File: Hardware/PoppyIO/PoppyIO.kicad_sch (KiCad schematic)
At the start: 244 parts, among them J1 WAGO 233-504, J10 Phoenix MPT 0,5/ 4-2,54, J11 TC2030-IDC, J12 Conn_02x06_Odd_Even, J2 WAGO 233-504, J3 WAGO 233-504, J4 WAGO 233-504, J5 WAGO 233-504, J6 WAGO 233-504, J7 WAGO 233-504, J8 WAGO 233-504, SW1 PTS645SH43SMTR92LFS, U1 Pico, U10 74HC14, U11 74HC14, U12 74HC14, U2 PCA9538PW, U3 PCA9538PW, U4 PCA9538PW, U5 PCA9538PW, U6 ULN2003AD, U7 ULN2003AD, U8 ULN2003AD, U9 74HC14

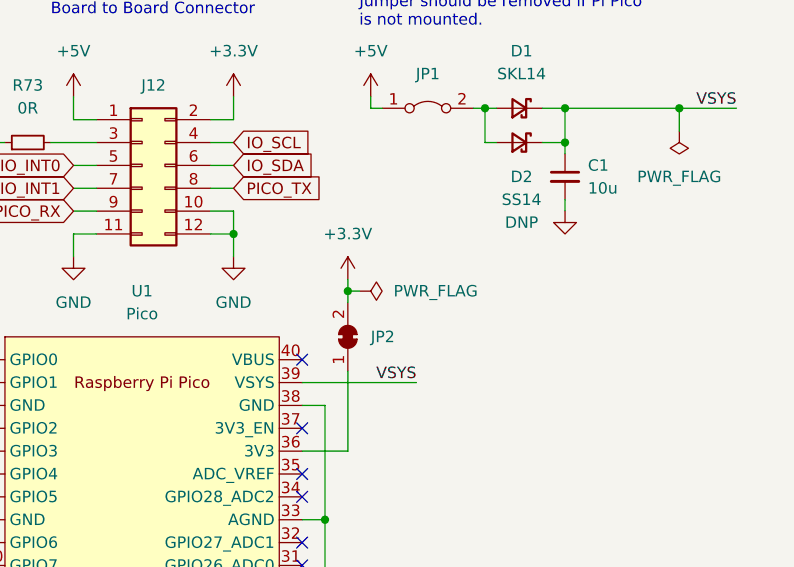
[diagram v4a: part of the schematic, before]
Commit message: hw: io: Update JP2
shouldn't be a solder jumper
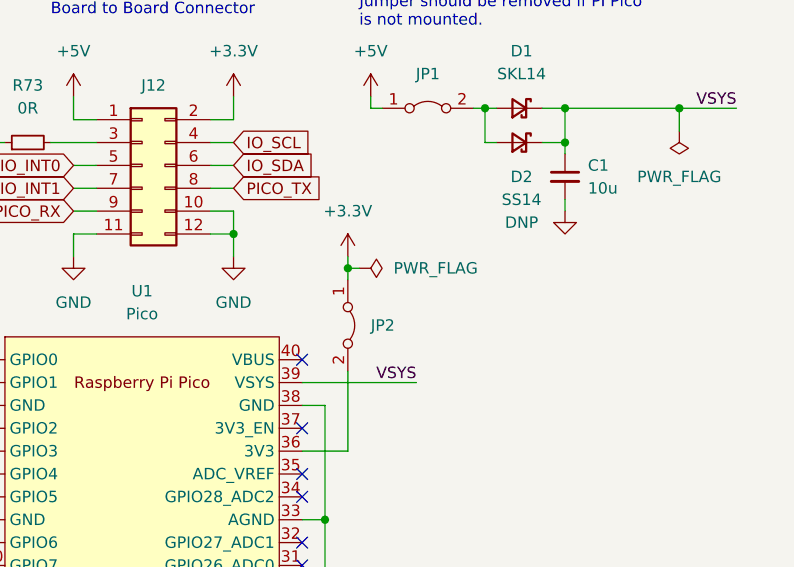
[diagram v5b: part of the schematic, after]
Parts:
- removed JP2: SolderJumper_2_Bridged, Jumper:SolderJumper-2_P1.3mm_Bridged_RoundedPad1.0x1.5mm, symbol Jumper:SolderJumper_2_Bridged
- added JP2: (no value), symbol Jumper:Jumper_2_Bridged
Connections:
- net +3V3: now also JP2.1 (A)
- net at U1.36 (3V3): now also JP2.2 (B)
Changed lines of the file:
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@@
   (junction (at 383.54 247.65) (diameter 0) (color 0 0 0 0)
   )
-  (junction (at 359.41 49.53) (diameter 0) (color 0 0 0 0)
+  (junction (at 359.41 46.99) (diameter 0) (color 0 0 0 0)
   )
   (junction (at 386.08 236.22) (diameter 0) (color 0 0 0 0)
@@
     (stroke (width 0) (type default) (color 0 0 0 0))
   )
-  (wire (pts (xy 359.41 49.53) (xy 360.68 49.53))
+  (wire (pts (xy 359.41 46.99) (xy 360.68 46.99))
     (stroke (width 0) (type default) (color 0 0 0 0))
   )
@@
     (stroke (width 0) (type default) (color 0 0 0 0))
   )
-  (wire (pts (xy 359.41 48.26) (xy 359.41 49.53))
+  (wire (pts (xy 359.41 45.72) (xy 359.41 46.99))
     (stroke (width 0) (type default) (color 0 0 0 0))
   )
@@
     (stroke (width 0) (type default) (color 0 0 0 0))
   )
-  (wire (pts (xy 359.41 49.53) (xy 359.41 50.8))
+  (wire (pts (xy 359.41 46.99) (xy 359.41 48.26))
     (stroke (width 0) (type default) (color 0 0 0 0))
   )
@@
     (pin "1")
   )
-  (symbol (lib_id "power:PWR_FLAG") (at 360.68 49.53 270) (unit 1)
+  (symbol (lib_id "power:PWR_FLAG") (at 360.68 46.99 270) (unit 1)
     (in_bom yes) (on_board yes) (fields_autoplaced)
-    (property "Reference" "#FLG0104" (id 0) (at 362.585 49.53 0)
+    (property "Reference" "#FLG0104" (id 0) (at 362.585 46.99 0)
       (effects (font (size 1.27 1.27)) hide)
     )
-    (property "Value" "PWR_FLAG" (id 1) (at 364.49 49.5299 90)
+    (property "Value" "PWR_FLAG" (id 1) (at 364.49 46.9899 90)
       (effects (font (size 1.27 1.27)) (justify left))
     )
-    (property "Footprint" "" (id 2) (at 360.68 49.53 0)
+    (property "Footprint" "" (id 2) (at 360.68 46.99 0)
       (effects (font (size 1.27 1.27)) hide)
     )
-    (property "Datasheet" "~" (id 3) (at 360.68 49.53 0)
+    (property "Datasheet" "~" (id 3) (at 360.68 46.99 0)
       (effects (font (size 1.27 1.27)) hide)
     )
@@
     (pin "1")
   )
-  (symbol (lib_id "power:+3.3V") (at 359.41 48.26 0) (unit 1)
+  (symbol (lib_id "power:+3.3V") (at 359.41 45.72 0) (unit 1)
     (in_bom yes) (on_board yes) (fields_autoplaced)
-    (property "Reference" "#PWR06" (id 0) (at 359.41 52.07 0)
+    (property "Reference" "#PWR06" (id 0) (at 359.41 49.53 0)
       (effects (font (size 1.27 1.27)) hide)
     )
-    (property "Value" "+3.3V" (id 1) (at 359.41 43.18 0))
-    (property "Footprint" "" (id 2) (at 359.41 48.26 0)
+    (property "Value" "+3.3V" (id 1) (at 359.41 40.64 0))
+    (property "Footprint" "" (id 2) (at 359.41 45.72 0)
       (effects (font (size 1.27 1.27)) hide)
     )
-    (property "Datasheet" "" (id 3) (at 359.41 48.26 0)
+    (property "Datasheet" "" (id 3) (at 359.41 45.72 0)
       (effects (font (size 1.27 1.27)) hide)
     )
@@
     (pin "7")
   )
-  (symbol (lib_id "Jumper:SolderJumper_2_Bridged") (at 359.41 54.61 270) (mirror x) (unit 1)
-    (in_bom yes) (on_board yes) (fields_autoplaced)
-    (property "Reference" "JP2" (id 0) (at 361.95 54.6099 90)
-      (effects (font (size 1.27 1.27)) (justify left))
-    )
-    (property "Value" "SolderJumper_2_Bridged" (id 1) (at 363.22 54.61 0)
-      (effects (font (size 1.27 1.27)) hide)
-    )
-    (property "Footprint" "Jumper:SolderJumper-2_P1.3mm_Bridged_RoundedPad1.0x1.5mm" (id 2) (at 359.41 54.61 0)
-      (effects (font (size 1.27 1.27)) hide)
-    )
-    (property "Datasheet" "~" (id 3) (at 359.41 54.61 0)
-      (effects (font (size 1.27 1.27)) hide)
-    )
-    (pin "1")
-    (pin "2")
-  )
   (symbol (lib_id "power:GND") (at 127 111.76 0) (unit 1)
     (in_bom yes) (on_board yes) (fields_autoplaced)
@@
     (pin "1")
   )
+  (symbol (lib_id "Jumper:Jumper_2_Bridged") (at 359.41 53.34 270) (unit 1)
+    (in_bom yes) (on_board yes) (fields_autoplaced)
+    (property "Reference" "JP2" (id 0) (at 361.95 53.3399 90)
+      (effects (font (size 1.27 1.27)) (justify left))
+    )
+    (property "Value" "" (id 1) (at 363.22 53.34 0)
+      (effects (font (size 1.27 1.27)) hide)
+    )
+    (property "Footprint" "" (id 2) (at 359.41 53.34 0)
+      (effects (font (size 1.27 1.27)) hide)
+    )
+    (property "Datasheet" "~" (id 3) (at 359.41 53.34 0)
+      (effects (font (size 1.27 1.27)) hide)
+    )
+    (pin "1")
+    (pin "2")
+  )
   (symbol (lib_id "Connector:TestPoint_Small") (at 66.04 228.6 0) (unit 1)
     (in_bom yes) (on_board yes)
@@
   (symbol (lib_id "power:+5V") (at 361.95 27.94 0) (unit 1)
     (in_bom yes) (on_board yes) (fields_autoplaced)
-    (property "Reference" "#PWR?" (id 0) (at 361.95 31.75 0)
+    (property "Reference" "#PWR0131" (id 0) (at 361.95 31.75 0)
       (effects (font (size 1.27 1.27)) hide)
     )
@@
       (reference "#PWR0130") (unit 1) (value "GND") (footprint "")
     )
+    (path "/f9200ee4-0053-410d-bc5c-53542c90d30e"
+      (reference "#PWR0131") (unit 1) (value "+5V") (footprint "")
+    )
     (path "/fb0963c8-0aa6-46ce-85a9-5d5af03b6001"
       (reference "#PWR0132") (unit 1) (value "+3.3V") (footprint "")
@@
       (reference "#PWR0143") (unit 1) (value "GND") (footprint "")
     )
-    (path "/f9200ee4-0053-410d-bc5c-53542c90d30e"
-      (reference "#PWR?") (unit 1) (value "+5V") (footprint "")
-    )
     (path "/b9ac49ae-7d34-4ed6-a926-b142ee48d81a"
       (reference "C1") (unit 1) (value "10u") (footprint "Capacitor_SMD:C_1210_3225Metric")
@@
       (reference "JP1") (unit 1) (value "~") (footprint "Connector_PinHeader_2.54mm:PinHeader_1x02_P2.54mm_Vertical")
     )
-    (path "/65d06c52-607b-438a-b9af-c2ce24e1e331"
-      (reference "JP2") (unit 1) (value "SolderJumper_2_Bridged") (footprint "Jumper:SolderJumper-2_P1.3mm_Bridged_RoundedPad1.0x1.5mm")
+    (path "/6612fd9a-51b0-4f77-bfea-9b018a73204f"
+      (reference "JP2") (unit 1) (value "~") (footprint "Connector_PinHeader_2.54mm:PinHeader_1x02_P2.54mm_Vertical")
     )
     (path "/d683efa9-3a6b-4bcc-9f90-fb444ca2faef"

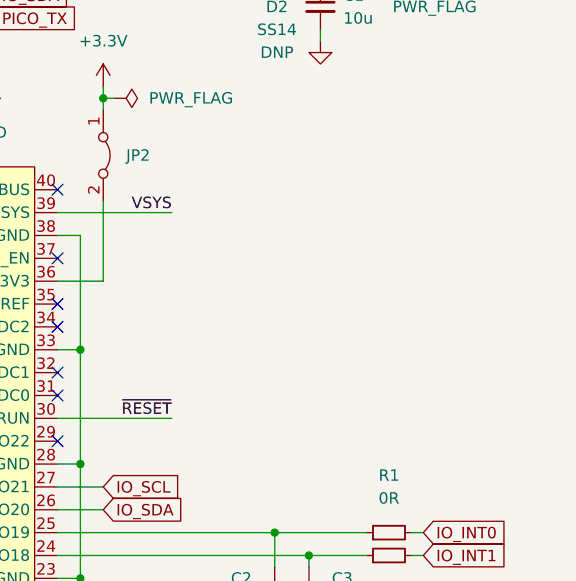
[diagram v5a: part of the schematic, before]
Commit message: hw: io: Add footprints for 3V3 decoupling caps
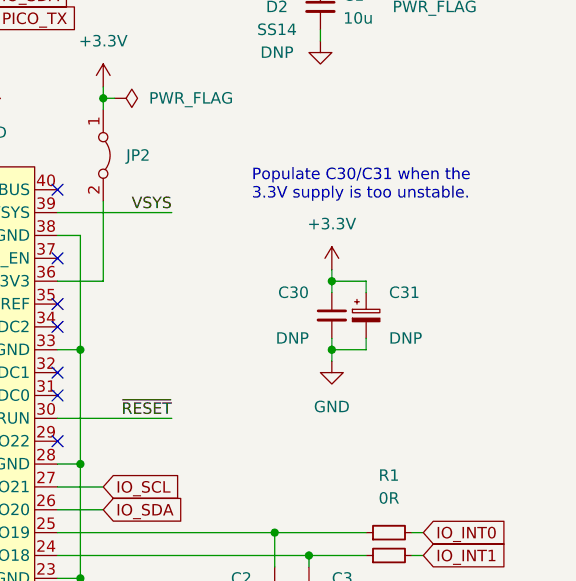
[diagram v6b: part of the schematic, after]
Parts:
- added C30: (no value), symbol Device:C_Small
- added C31: (no value), symbol Device:C_Polarized_Small
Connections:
- net +3V3: now also C30.1, C31.1
- net GND: now also C30.2, C31.2
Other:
- note added: "Populate C30/C31 when the 3.3V supply is too unstable."
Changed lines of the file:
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@@
   (junction (at 256.54 182.88) (diameter 0) (color 0 0 0 0)
   )
+  (junction (at 384.81 67.31) (diameter 0) (color 0 0 0 0)
+  )
   (junction (at 255.27 231.14) (diameter 0) (color 0 0 0 0)
   )
@@
   (junction (at 295.91 144.78) (diameter 0) (color 0 0 0 0)
   )
+  (junction (at 384.81 74.93) (diameter 0) (color 0 0 0 0)
+  )
   (junction (at 396.24 151.13) (diameter 0) (color 0 0 0 0)
   )
@@
     (stroke (width 0) (type default) (color 0 0 0 0))
   )
+  (wire (pts (xy 384.81 74.93) (xy 388.62 74.93))
+    (stroke (width 0) (type default) (color 0 0 0 0))
+  )
   (wire (pts (xy 186.69 255.27) (xy 187.96 255.27))
     (stroke (width 0) (type default) (color 0 0 0 0))
@@
     (stroke (width 0) (type default) (color 0 0 0 0))
   )
+  (wire (pts (xy 384.81 67.31) (xy 388.62 67.31))
+    (stroke (width 0) (type default) (color 0 0 0 0))
+  )
   (wire (pts (xy 243.84 255.27) (xy 245.11 255.27))
     (stroke (width 0) (type default) (color 0 0 0 0))
@@
     (stroke (width 0) (type default) (color 0 0 0 0))
   )
+  (wire (pts (xy 384.81 66.04) (xy 384.81 67.31))
+    (stroke (width 0) (type default) (color 0 0 0 0))
+  )
   (wire (pts (xy 255.27 241.3) (xy 251.46 241.3))
     (stroke (width 0) (type default) (color 0 0 0 0))
@@
     (stroke (width 0) (type default) (color 0 0 0 0))
   )
+  (wire (pts (xy 388.62 67.31) (xy 388.62 68.58))
+    (stroke (width 0) (type default) (color 0 0 0 0))
+  )
   (wire (pts (xy 210.82 229.87) (xy 210.82 231.14))
     (stroke (width 0) (type default) (color 0 0 0 0))
@@
     (stroke (width 0) (type default) (color 0 0 0 0))
   )
+  (wire (pts (xy 388.62 73.66) (xy 388.62 74.93))
+    (stroke (width 0) (type default) (color 0 0 0 0))
+  )
   (wire (pts (xy 82.55 95.25) (xy 82.55 105.41))
     (stroke (width 0) (type default) (color 0 0 0 0))
@@
     (stroke (width 0) (type default) (color 0 0 0 0))
   )
+  (wire (pts (xy 384.81 68.58) (xy 384.81 67.31))
+    (stroke (width 0) (type default) (color 0 0 0 0))
+  )
   (wire (pts (xy 194.31 41.91) (xy 195.58 41.91))
     (stroke (width 0) (type default) (color 0 0 0 0))
@@
     (stroke (width 0) (type default) (color 0 0 0 0))
   )
+  (wire (pts (xy 384.81 74.93) (xy 384.81 76.2))
+    (stroke (width 0) (type default) (color 0 0 0 0))
+  )
   (polyline (pts (xy 290.83 67.31) (xy 290.83 88.9))
     (stroke (width 0) (type default) (color 0 0 0 0))
@@
     (stroke (width 0) (type default) (color 0 0 0 0))
   )
+  (wire (pts (xy 384.81 73.66) (xy 384.81 74.93))
+    (stroke (width 0) (type default) (color 0 0 0 0))
+  )
   (wire (pts (xy 149.86 95.25) (xy 153.67 95.25))
     (stroke (width 0) (type default) (color 0 0 0 0))
@@
     (effects (font (size 1.27 1.27)) (justify right bottom))
   )
+  (text "Populate C30/C31 when the\n3.3V supply is too unstable."
+    (at 375.92 58.42 0)
+    (effects (font (size 1.27 1.27)) (justify left bottom))
+  )
   (text "V_{f}≅2.4V\nI=1mA" (at 91.44 172.72 0)
     (effects (font (size 1.27 1.27)) (justify left bottom))
@@
     (pin "1")
   )
+  (symbol (lib_id "power:+3.3V") (at 384.81 66.04 0) (unit 1)
+    (in_bom yes) (on_board yes) (fields_autoplaced)
+    (property "Reference" "#PWR094" (id 0) (at 384.81 69.85 0)
+      (effects (font (size 1.27 1.27)) hide)
+    )
+    (property "Value" "+3.3V" (id 1) (at 384.81 60.96 0))
+    (property "Footprint" "" (id 2) (at 384.81 66.04 0)
+      (effects (font (size 1.27 1.27)) hide)
+    )
+    (property "Datasheet" "" (id 3) (at 384.81 66.04 0)
+      (effects (font (size 1.27 1.27)) hide)
+    )
+    (pin "1")
+  )
   (symbol (lib_id "power:GND") (at 334.01 240.03 0) (unit 1)
     (in_bom yes) (on_board yes) (fields_autoplaced)
@@
     (pin "9")
   )
+  (symbol (lib_id "Device:C_Small") (at 384.81 71.12 0) (unit 1)
+    (in_bom yes) (on_board yes) (fields_autoplaced)
+    (property "Reference" "C30" (id 0) (at 382.27 68.5862 0)
+      (effects (font (size 1.27 1.27)) (justify right))
+    )
+    (property "Value" "" (id 1) (at 382.27 71.1262 0)
+      (effects (font (size 1.27 1.27)) (justify right))
+    )
+    (property "Footprint" "" (id 2) (at 384.81 71.12 0)
+      (effects (font (size 1.27 1.27)) hide)
+    )
+    (property "Datasheet" "~" (id 3) (at 384.81 71.12 0)
+      (effects (font (size 1.27 1.27)) hide)
+    )
+    (property "Config" "DNP" (id 4) (at 382.27 73.6662 0)
+      (effects (font (size 1.27 1.27)) (justify right))
+    )
+    (pin "1")
+    (pin "2")
+  )
   (symbol (lib_id "Device:LED_Small") (at 83.82 196.85 90) (unit 1)
     (in_bom yes) (on_board yes) (fields_autoplaced)
@@
     (pin "2")
   )
+  (symbol (lib_id "power:GND") (at 384.81 76.2 0) (unit 1)
+    (in_bom yes) (on_board yes) (fields_autoplaced)
+    (property "Reference" "#PWR096" (id 0) (at 384.81 82.55 0)
+      (effects (font (size 1.27 1.27)) hide)
+    )
+    (property "Value" "GND" (id 1) (at 384.81 81.28 0))
+    (property "Footprint" "" (id 2) (at 384.81 76.2 0)
+      (effects (font (size 1.27 1.27)) hide)
+    )
+    (property "Datasheet" "" (id 3) (at 384.81 76.2 0)
+      (effects (font (size 1.27 1.27)) hide)
+    )
+    (pin "1")
+  )
   (symbol (lib_id "power:GND") (at 128.27 242.57 0) (unit 1)
     (in_bom yes) (on_board yes) (fields_autoplaced)
@@
     (pin "1")
   )
+  (symbol (lib_id "Device:C_Polarized_Small") (at 388.62 71.12 0) (unit 1)
+    (in_bom yes) (on_board yes) (fields_autoplaced)
+    (property "Reference" "C31" (id 0) (at 391.16 68.5862 0)
+      (effects (font (size 1.27 1.27)) (justify left))
+    )
+    (property "Value" "" (id 1) (at 391.16 71.1262 0)
+      (effects (font (size 1.27 1.27)) (justify left))
+    )
+    (property "Footprint" "" (id 2) (at 388.62 71.12 0)
+      (effects (font (size 1.27 1.27)) hide)
+    )
+    (property "Datasheet" "~" (id 3) (at 388.62 71.12 0)
+      (effects (font (size 1.27 1.27)) hide)
+    )
+    (property "Config" "DNP" (id 4) (at 391.16 73.6662 0)
+      (effects (font (size 1.27 1.27)) (justify left))
+    )
+    (pin "1")
+    (pin "2")
+  )
   (symbol (lib_id "Device:R_Small") (at 83.82 227.33 180) (unit 1)
     (in_bom yes) (on_board yes) (fields_autoplaced)
@@
       (reference "#PWR093") (unit 1) (value "GND") (footprint "")
     )
+    (path "/9dd191db-8da1-44f7-8a7b-1e3f961df059"
+      (reference "#PWR094") (unit 1) (value "+3.3V") (footprint "")
+    )
     (path "/847edd97-51c8-496d-aea6-58fc2dedc1e7"
       (reference "#PWR095") (unit 1) (value "+24V") (footprint "")
     )
+    (path "/daa2bf8b-4a53-4a4f-9c41-9a9794c9135b"
+      (reference "#PWR096") (unit 1) (value "GND") (footprint "")
+    )
     (path "/c9dff289-8fb3-4dc3-ad7b-1ec4d4cc6f61"
       (reference "#PWR097") (unit 1) (value "+24V") (footprint "")
@@
       (reference "C29") (unit 1) (value "100n") (footprint "Capacitor_SMD:C_0603_1608Metric_Pad1.08x0.95mm_HandSolder")
     )
+    (path "/d0413f23-7afe-492d-b296-27327d2380b5"
+      (reference "C30") (unit 1) (value "10u") (footprint "Capacitor_SMD:C_1210_3225Metric")
+    )
+    (path "/db736eab-c78b-40a8-8adf-dcc2124cb799"
+      (reference "C31") (unit 1) (value "10u") (footprint "Capacitor_THT:CP_Radial_D5.0mm_P2.50mm")
+    )
     (path "/63c9d624-6a70-47f9-97f3-de868d5c5c25"

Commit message: hw: io: Add artwork
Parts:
- added SYM1: (no value), symbol PoppyLogicController:SYM_Rahix
- C30: value (none) -> 10u; footprint (none) -> Capacitor_SMD:C_1210_3225Metric
- C31: value (none) -> 10u; footprint (none) -> Capacitor_THT:CP_Radial_D5.0mm_P2.50mm
- J9: value (none) -> Phoenix MPT 0,5/ 4-2,54; footprint (none) -> TerminalBlock_Phoenix:TerminalBlock_Phoenix_MPT-0,5-4-2.54_1x04_P2.54mm_Horizontal
- JP2: value (none) -> ~; footprint (none) -> Connector_PinHeader_2.54mm:PinHeader_1x02_P2.54mm_Vertical
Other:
- moved on the sheet: C27, C28, J11, JP11, R69, R70, R71, R72, SW1, TP35, TP36, TP37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

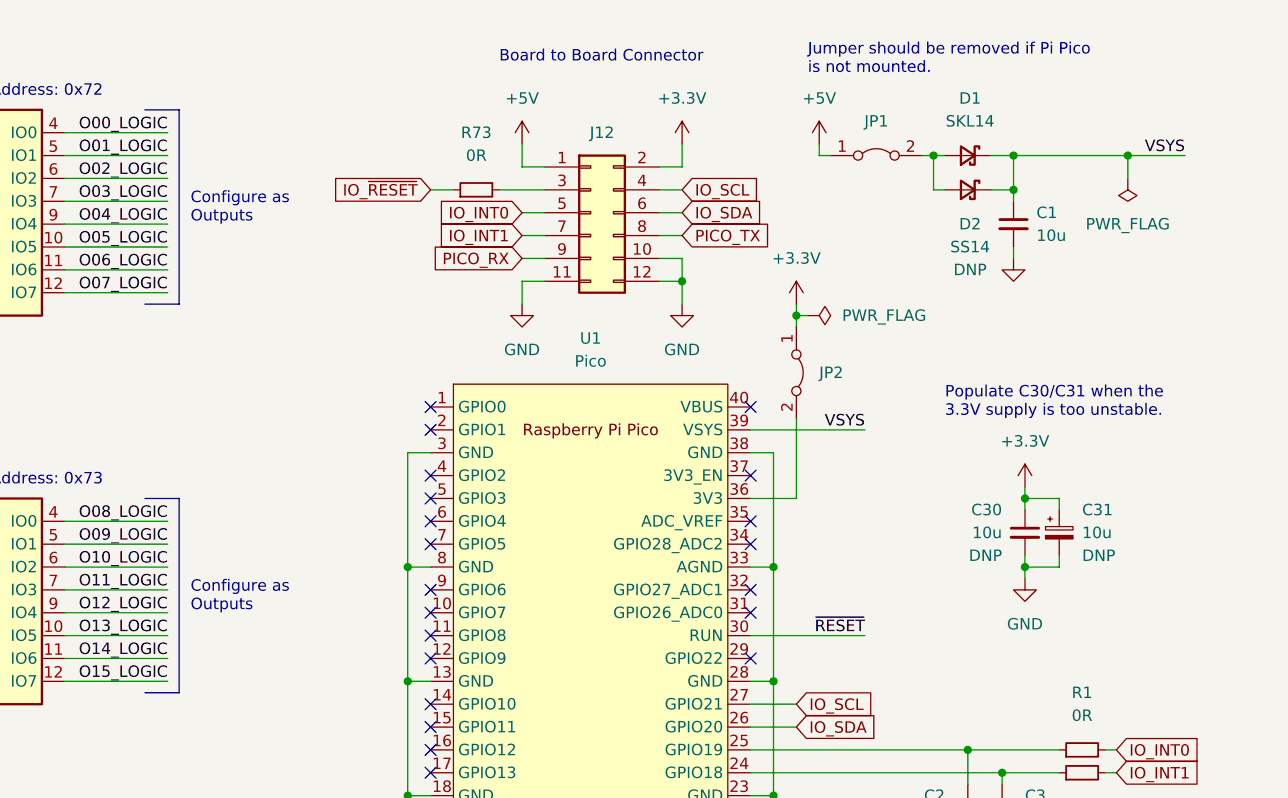
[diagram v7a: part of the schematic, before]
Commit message: hw: io: Add footprints for 24V -> 5V regulator
In the future, maybe we will want to switch to a unified 24V supply.
Add footprints for installing a regulator or SPMS to do this.
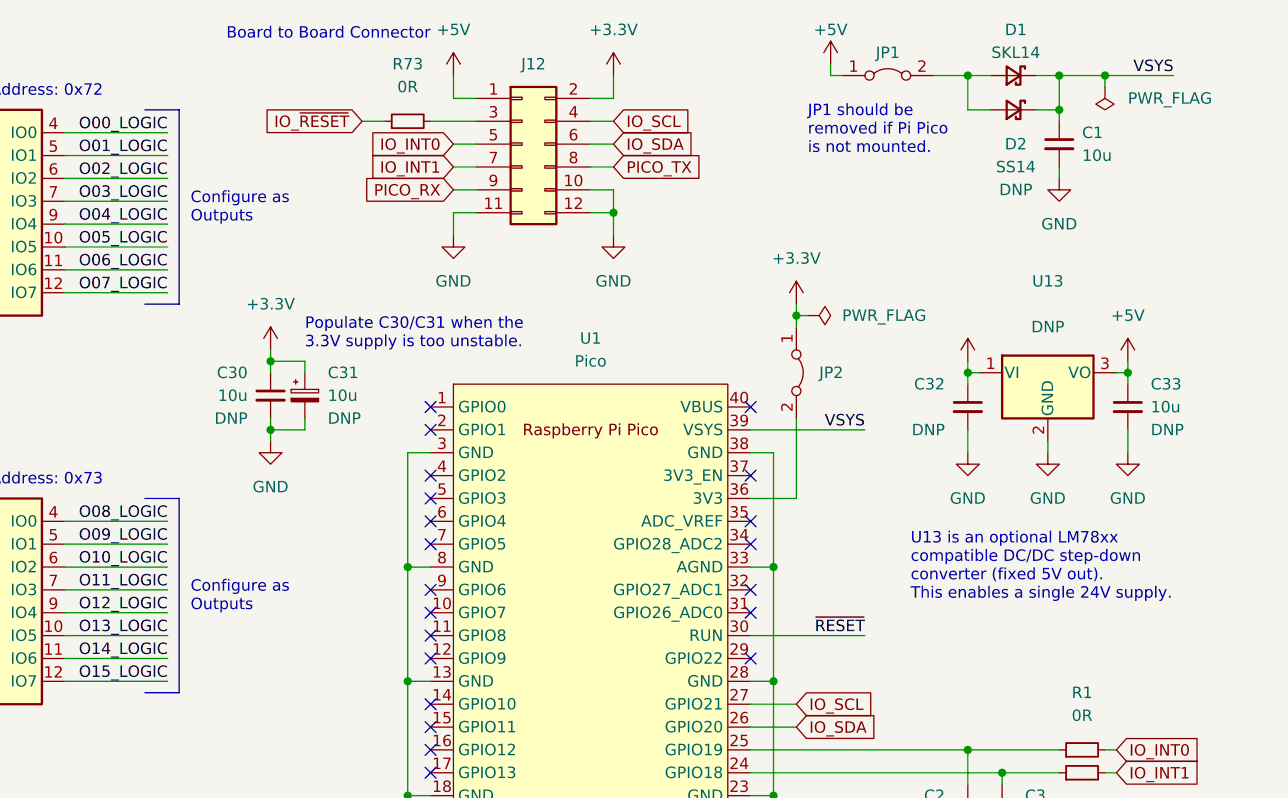
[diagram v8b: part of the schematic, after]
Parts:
- added C32: (no value), symbol Device:C_Small
- added C33: 10u, Capacitor_SMD:C_1210_3225Metric, symbol Device:C_Small
- added U13: (no value), symbol Regulator_Linear:LM7805_TO220
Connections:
- net +24V: now also C32.1, U13.1 (VI)
- net +5V: now also C33.1, U13.3 (VO)
- net GND: now also C32.2, C33.2, U13.2 (GND)
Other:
- note added: "JP1 should be removed if Pi Pico is not mounted."
- note added: "U13 is an optional LM78xx compatible DC/DC step-down converter (fixed 5V out). This enables a single 24V supply."
- note removed: "Jumper should be removed if Pi Pico is not mounted."
- moved on the sheet: C1, C30, C31, D1, D2, J12, JP1, R73
